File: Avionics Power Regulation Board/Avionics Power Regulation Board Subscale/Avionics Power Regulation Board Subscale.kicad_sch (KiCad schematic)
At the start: 11 parts, among them J1 Conn_01x04_Socket, J2 Conn_01x06_Socket, U1 SC0917

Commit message: added radio
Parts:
- added J3: Conn_01x06_Socket, Connector_PinSocket_2.54mm:PinSocket_1x06_P2.54mm_Horizontal, symbol Connector:Conn_01x06_Socket
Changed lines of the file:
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@@
+		)
+	)
+	(rectangle
+		(start 99.06 97.79)
+		(end 158.75 121.92)
+		(stroke
+			(width 0)
+			(type default)
+		)
+		(fill
+			(type none)
 		)
 	)
@@
 					(unit 1)
 				)
+			)
+		)
+	)
+	(symbol
+		(lib_id "Connector:Conn_01x06_Socket")
+		(at 113.03 109.22 0)
+		(unit 1)
+		(exclude_from_sim no)
+		(in_bom yes)
+		(on_board yes)
+		(dnp no)
+		(property "Reference" "J3"
+			(at 113.792 108.966 0)
+			(effects
+				(font
+					(size 1.27 1.27)
+				)
+				(justify left)
+			)
+		)
+		(property "Value" "Conn_01x06_Socket"
+			(at 114.3 111.7599 0)
+			(effects
+				(font
+					(size 1.27 1.27)
+				)
+				(justify left)
+			)
+		)
+		(property "Footprint" "Connector_PinSocket_2.54mm:PinSocket_1x06_P2.54mm_Horizontal"
+			(at 113.03 109.22 0)
+			(effects
+				(font
+					(size 1.27 1.27)
+				)
+				(hide yes)
+			)
+		)
+		(property "Datasheet" "~"
+			(at 113.03 109.22 0)
+			(effects
+				(font
+					(size 1.27 1.27)
+				)
+				(hide yes)
+			)
+		)
+		(property "Description" "Generic connector, single row, 01x06, script generated"
+			(at 113.03 109.22 0)
+			(effects
+				(font
+					(size 1.27 1.27)
+				)
+				(hide yes)
+			)
+		)
+		(property "Purpose" "RYLR896"
+			(at 103.124 96.266 0)
+			(effects
+				(font
+					(size 1.27 1.27)
+				)
+			)
+		)
+		(pin "5"
+		)
+		(pin "2"
+		)
+		(pin "1"
+		)
+		(pin "3"
+		)
+		(pin "4"
+		)
+		(pin "6"
+		)
+		(instances
+			(project ""
+				(path "/96c718b9-ba1d-44c9-9433-65018c8a3882"
+					(reference "J3")
+					(unit 1)
+				)

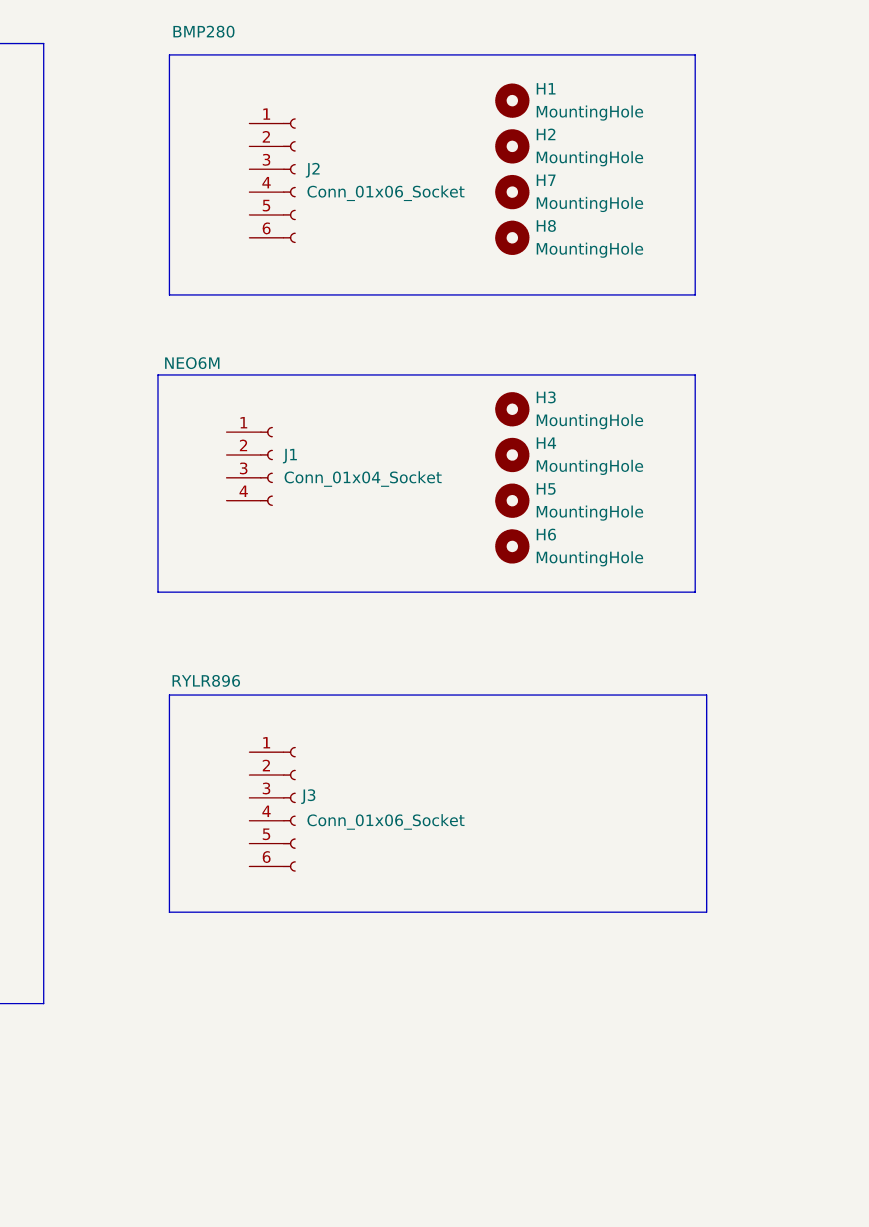
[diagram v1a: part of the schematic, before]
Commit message: Added Accurate footprints
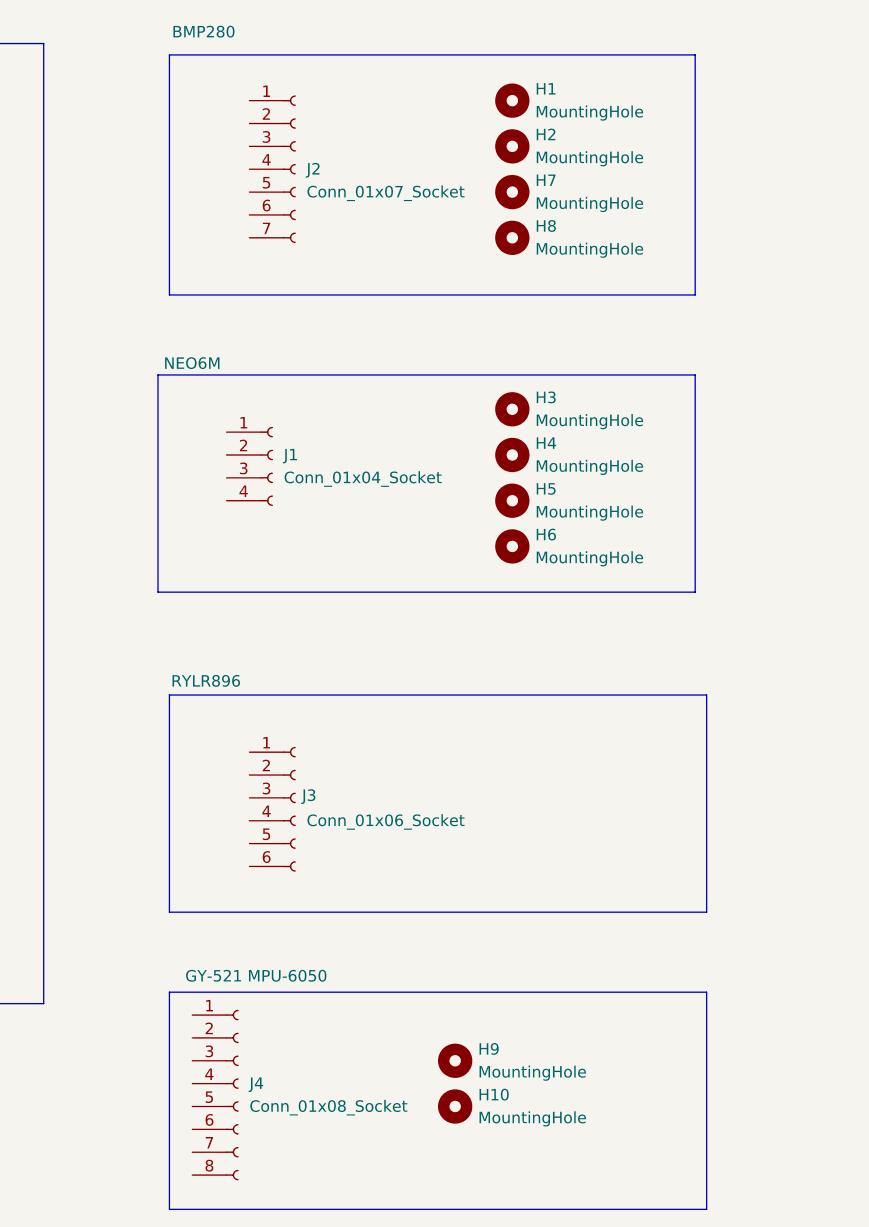
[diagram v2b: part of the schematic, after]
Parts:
- added H10, H9: MountingHole, MountingHole:MountingHole_2.1mm, symbol Mechanical:MountingHole
- added J4: Conn_01x08_Socket, Connector_PinSocket_2.54mm:PinSocket_1x08_P2.54mm_Vertical, symbol Connector:Conn_01x08_Socket
- J2: value Conn_01x06_Socket -> Conn_01x07_Socket; footprint Connector_PinSocket_2.54mm:PinSocket_1x06_P2.54mm_Vertical -> Connector_PinSocket_2.54mm:PinSocket_1x07_P2.54mm_Vertical; symbol Connector:Conn_01x06_Socket -> Connector:Conn_01x07_Socket
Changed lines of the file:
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@@
 		)
 	)
+	(rectangle
+		(start 99.06 130.81)
+		(end 158.75 154.94)
+		(stroke
+			(width 0)
+			(type default)
+		)
+		(fill
+			(type none)
+		)
+	)
 	(image
 		(at 236.855 54.61)
@@
 	)
 	(symbol
-		(lib_id "Connector:Conn_01x06_Socket")
+		(lib_id "Connector:Conn_01x07_Socket")
 		(at 113.03 39.37 0)
 		(unit 1)
@@
 			)
 		)
-		(property "Value" "Conn_01x06_Socket"
+		(property "Value" "Conn_01x07_Socket"
 			(at 114.3 41.9099 0)
 			(effects
@@
 			)
 		)
-		(property "Footprint" "Connector_PinSocket_2.54mm:PinSocket_1x06_P2.54mm_Vertical"
+		(property "Footprint" "Connector_PinSocket_2.54mm:PinSocket_1x07_P2.54mm_Vertical"
 			(at 113.03 39.37 0)
 			(effects
@@
 			)
 		)
-		(property "Description" "Generic connector, single row, 01x06, script generated"
+		(property "Description" "Generic connector, single row, 01x07, script generated"
 			(at 113.03 39.37 0)
 			(effects
@@
 		(pin "1"
 		)
+		(pin "7"
+		)
 		(instances
 			(project "Avionics Power Regulation Board Subscale"
@@
 	)
 	(symbol
+		(lib_id "Mechanical:MountingHole")
+		(at 130.81 138.43 0)
+		(unit 1)
+		(exclude_from_sim yes)
+		(in_bom no)
+		(on_board yes)
+		(dnp no)
+		(fields_autoplaced yes)
+		(property "Reference" "H9"
+			(at 133.35 137.1599 0)
+			(effects
+				(font
+					(size 1.27 1.27)
+				)
+				(justify left)
+			)
+		)
+		(property "Value" "MountingHole"
+			(at 133.35 139.6999 0)
+			(effects
+				(font
+					(size 1.27 1.27)
+				)
+				(justify left)
+			)
+		)
+		(property "Footprint" "MountingHole:MountingHole_2.1mm"
+			(at 130.81 138.43 0)
+			(effects
+				(font
+					(size 1.27 1.27)
+				)
+				(hide yes)
+			)
+		)
+		(property "Datasheet" "~"
+			(at 130.81 138.43 0)
+			(effects
+				(font
+					(size 1.27 1.27)
+				)
+				(hide yes)
+			)
+		)
+		(property "Description" "Mounting Hole without connection"
+			(at 130.81 138.43 0)
+			(effects
+				(font
+					(size 1.27 1.27)
+				)
+				(hide yes)
+			)
+		)
+		(instances
+			(project "Avionics Power Regulation Board Subscale"
+				(path "/96c718b9-ba1d-44c9-9433-65018c8a3882"
+					(reference "H9")
+					(unit 1)
+				)
+			)
+		)
+	)
+	(symbol
 		(lib_id "Connector:Conn_01x04_Socket")
 		(at 110.49 71.12 0)
@@
 					(unit 1)
 				)
+			)
+		)
+	)
+	(symbol
+		(lib_id "Connector:Conn_01x08_Socket")
+		(at 106.68 140.97 0)
+		(unit 1)
+		(exclude_from_sim no)
+		(in_bom yes)
+		(on_board yes)
+		(dnp no)
+		(property "Reference" "J4"
+			(at 107.95 140.9699 0)
+			(effects
+				(font
+					(size 1.27 1.27)
+				)
+				(justify left)
+			)
+		)
+		(property "Value" "Conn_01x08_Socket"
+			(at 107.95 143.5099 0)
+			(effects
+				(font
+					(size 1.27 1.27)
+				)
+				(justify left)
+			)
+		)
+		(property "Footprint" "Connector_PinSocket_2.54mm:PinSocket_1x08_P2.54mm_Vertical"
+			(at 106.68 140.97 0)
+			(effects
+				(font
+					(size 1.27 1.27)
+				)
+				(hide yes)
+			)
+		)
+		(property "Datasheet" "~"
+			(at 106.68 140.97 0)
+			(effects
+				(font
+					(size 1.27 1.27)
+				)
+				(hide yes)
+			)
+		)
+		(property "Description" "Generic connector, single row, 01x08, script generated"
+			(at 106.68 140.97 0)
+			(effects
+				(font
+					(size 1.27 1.27)
+				)
+				(hide yes)
+			)
+		)
+		(property "Purpose" "GY-521 MPU-6050"
+			(at 108.712 129.032 0)
+			(effects
+				(font
+					(size 1.27 1.27)
+				)
+			)
+		)
+		(pin "4"
+		)
+		(pin "2"
+		)
+		(pin "8"
+		)
+		(pin "7"
+		)
+		(pin "5"
+		)
+		(pin "6"
+		)
+		(pin "1"
+		)
+		(pin "3"
+		)
+		(instances
+			(project ""
+				(path "/96c718b9-ba1d-44c9-9433-65018c8a3882"
+					(reference "J4")
+					(unit 1)
+				)
+			)
+		)
+	)
+	(symbol
+		(lib_id "Mechanical:MountingHole")
+		(at 130.81 143.51 0)
+		(unit 1)
+		(exclude_from_sim yes)
+		(in_bom no)
+		(on_board yes)
+		(dnp no)
+		(fields_autoplaced yes)
+		(property "Reference" "H10"
+			(at 133.35 142.2399 0)
+			(effects
+				(font
+					(size 1.27 1.27)
+				)
+				(justify left)
+			)
+		)
+		(property "Value" "MountingHole"
+			(at 133.35 144.7799 0)
+			(effects
+				(font
+					(size 1.27 1.27)
+				)
+				(justify left)
+			)
+		)
+		(property "Footprint" "MountingHole:MountingHole_2.1mm"
+			(at 130.81 143.51 0)
+			(effects
+				(font
+					(size 1.27 1.27)
+				)
+				(hide yes)
+			)
+		)
+		(property "Datasheet" "~"
+			(at 130.81 143.51 0)
+			(effects
+				(font
+					(size 1.27 1.27)
+				)
+				(hide yes)
+			)
+		)
+		(property "Description" "Mounting Hole without connection"
+			(at 130.81 143.51 0)
+			(effects
+				(font
+					(size 1.27 1.27)
+				)
+				(hide yes)
+			)
+		)
+		(instances
+			(project "Avionics Power Regulation Board Subscale"
+				(path "/96c718b9-ba1d-44c9-9433-65018c8a3882"
+					(reference "H10")
+					(unit 1)
+				)

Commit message: Small PCB Edits
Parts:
- removed H8: MountingHole, MountingHole:MountingHole_2.1mm, symbol Mechanical:MountingHole
- added J5: Conn_01x05_Socket, Connector_PinSocket_2.54mm:PinSocket_1x05_P2.54mm_Vertical, symbol Connector:Conn_01x05_Socket
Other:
- moved on the sheet: H7
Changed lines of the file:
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@@
 	)
 	(rectangle
+		(start 20.32 147.32)
+		(end 63.5 168.91)
+		(stroke
+			(width 0)
+			(type default)
+		)
+		(fill
+			(type none)
+		)
+	)
+	(rectangle
 		(start 97.79 62.23)
 		(end 157.48 86.36)
@@
 	)
 	(symbol
-		(lib_id "Mechanical:MountingHole")
-		(at 137.16 46.99 0)
-		(unit 1)
-		(exclude_from_sim yes)
-		(in_bom no)
-		(on_board yes)
-		(dnp no)
-		(fields_autoplaced yes)
-		(property "Reference" "H8"
-			(at 139.7 45.7199 0)
-			(effects
-				(font
-					(size 1.27 1.27)
-				)
-				(justify left)
-			)
-		)
-		(property "Value" "MountingHole"
-			(at 139.7 48.2599 0)
-			(effects
-				(font
-					(size 1.27 1.27)
-				)
-				(justify left)
-			)
-		)
-		(property "Footprint" "MountingHole:MountingHole_2.1mm"
-			(at 137.16 46.99 0)
-			(effects
-				(font
-					(size 1.27 1.27)
-				)
-				(hide yes)
-			)
-		)
-		(property "Datasheet" "~"
-			(at 137.16 46.99 0)
-			(effects
-				(font
-					(size 1.27 1.27)
-				)
-				(hide yes)
-			)
-		)
-		(property "Description" "Mounting Hole without connection"
-			(at 137.16 46.99 0)
-			(effects
-				(font
-					(size 1.27 1.27)
-				)
-				(hide yes)
-			)
-		)
-		(instances
-			(project "Avionics Power Regulation Board Subscale"
-				(path "/96c718b9-ba1d-44c9-9433-65018c8a3882"
-					(reference "H8")
-					(unit 1)
-				)
-			)
-		)
-	)
-	(symbol
 		(lib_id "Connector:Conn_01x07_Socket")
 		(at 113.03 39.37 0)
@@
 	(symbol
 		(lib_id "Mechanical:MountingHole")
-		(at 137.16 41.91 0)
+		(at 137.16 36.83 0)
 		(unit 1)
 		(exclude_from_sim yes)
@@
 		(fields_autoplaced yes)
 		(property "Reference" "H7"
-			(at 139.7 40.6399 0)
+			(at 139.7 35.5599 0)
 			(effects
 				(font
@@
 		)
 		(property "Value" "MountingHole"
-			(at 139.7 43.1799 0)
+			(at 139.7 38.0999 0)
 			(effects
 				(font
@@
 		)
 		(property "Footprint" "MountingHole:MountingHole_2.1mm"
-			(at 137.16 41.91 0)
+			(at 137.16 36.83 0)
 			(effects
 				(font
@@
 		)
 		(property "Datasheet" "~"
-			(at 137.16 41.91 0)
+			(at 137.16 36.83 0)
 			(effects
 				(font
@@
 		)
 		(property "Description" "Mounting Hole without connection"
-			(at 137.16 41.91 0)
+			(at 137.16 36.83 0)
 			(effects
 				(font
@@
 	)
 	(symbol
+		(lib_id "Mechanical:MountingHole")
+		(at 22.86 149.86 0)
+		(unit 1)
+		(exclude_from_sim yes)
+		(in_bom no)
+		(on_board yes)
+		(dnp no)
+		(fields_autoplaced yes)
+		(property "Reference" "H2"
+			(at 25.4 148.5899 0)
+			(effects
+				(font
+					(size 1.27 1.27)
+				)
+				(justify left)
+			)
+		)
+		(property "Value" "MountingHole"
+			(at 25.4 151.1299 0)
+			(effects
+				(font
+					(size 1.27 1.27)
+				)
+				(justify left)
+			)
+		)
+		(property "Footprint" "MountingHole:MountingHole_2.1mm"
+			(at 22.86 149.86 0)
+			(effects
+				(font
+					(size 1.27 1.27)
+				)
+				(hide yes)
+			)
+		)
+		(property "Datasheet" "~"
+			(at 22.86 149.86 0)
+			(effects
+				(font
+					(size 1.27 1.27)
+				)
+				(hide yes)
+			)
+		)
+		(property "Description" "Mounting Hole without connection"
+			(at 22.86 149.86 0)
+			(effects
+				(font
+					(size 1.27 1.27)
+				)
+				(hide yes)
+			)
+		)
+		(instances
+			(project "Avionics Power Regulation Board Subscale"
+				(path "/96c718b9-ba1d-44c9-9433-65018c8a3882"
+					(reference "H2")
+					(unit 1)
+				)
+			)
+		)
+	)
+	(symbol
 		(lib_id "SC0917:SC0917")
 		(at 50.8 77.47 0)
@@
 	)
 	(symbol
-		(lib_id "Mechanical:MountingHole")
-		(at 137.16 36.83 0)
+		(lib_id "Connector:Conn_01x05_Socket")
+		(at 41.91 158.75 0)
 		(unit 1)
-		(exclude_from_sim yes)
-		(in_bom no)
+		(exclude_from_sim no)
+		(in_bom yes)
 		(on_board yes)
 		(dnp no)
-		(fields_autoplaced yes)
-		(property "Reference" "H2"
-			(at 139.7 35.5599 0)
+		(property "Reference" "J5"
+			(at 43.18 157.4799 0)
 			(effects
 				(font
@@
 			)
 		)
-		(property "Value" "MountingHole"
-			(at 139.7 38.0999 0)
+		(property "Value" "Conn_01x05_Socket"
+			(at 43.18 160.0199 0)
 			(effects
 				(font
@@
 			)
 		)
-		(property "Footprint" "MountingHole:MountingHole_2.1mm"
-			(at 137.16 36.83 0)
+		(property "Footprint" "Connector_PinSocket_2.54mm:PinSocket_1x05_P2.54mm_Vertical"
+			(at 41.91 158.75 0)
 			(effects
 				(font
@@
 		)
 		(property "Datasheet" "~"
-			(at 137.16 36.83 0)
+			(at 41.91 158.75 0)
 			(effects
 				(font
@@
 			)
 		)
-		(property "Description" "Mounting Hole without connection"
-			(at 137.16 36.83 0)
+		(property "Description" "Generic connector, single row, 01x05, script generated"
+			(at 41.91 158.75 0)
 			(effects
 				(font
@@
 			)
 		)
+		(property "Purpose" "Battery Board Connection"
+			(at 45.72 146.05 0)
+			(effects
+				(font
+					(size 1.27 1.27)
+				)
+			)
+		)
+		(pin "5"
+		)
+		(pin "4"
+		)
+		(pin "2"
+		)
+		(pin "3"
+		)
+		(pin "1"
+		)
 		(instances
-			(project "Avionics Power Regulation Board Subscale"
+			(project ""
 				(path "/96c718b9-ba1d-44c9-9433-65018c8a3882"
-					(reference "H2")
+					(reference "J5")
 					(unit 1)
 				)
